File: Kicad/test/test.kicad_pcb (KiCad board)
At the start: 2 copper layers, 50 x 50 mm, 69 parts, among them J1 SPKOUT, J2 PrgmUART, P1 USB_C_Plug_USB2.0, SW1 SW_Push, SW2 SW_Push, SW3 SW_Push, SW4 SW_Push, SW5 SW_Push, U1 MAX98357A, U2 ESP32-S3-WROOM-1

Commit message: Started PCB Layout designs
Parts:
- moved SW2 0.45 mm to (159.5, 120.5)
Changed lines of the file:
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@@
 	(footprint "switchLibrary:K2-1114SA-A4SW-06"
 		(layer "F.Cu")
-		(at 159.898871 120.51318 -150)
+		(at 159.455129 120.467423 -150)
 		(property "Reference" "SW2"
 			(at 0 -3.83 30)

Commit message: Placed components on PCB
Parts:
- C1, C10, C11, C12, C13, C14, C15, C16, C17, C18, C19, C2, C20, C21, C22, C23, C24, C25, C26, C27, C28, C29, C3, C30, C4, C5, C6, C7, C8, C9, L1, L2: footprint Capacitor_SMD:C_0805_2012Metric_Pad1.18x1.45mm_HandSolder -> Capacitor_SMD:C_0603_1608Metric_Pad1.08x0.95mm_HandSolder
- J2: footprint Connector_PinHeader_2.54mm:PinHeader_1x06_P2.54mm_Vertical -> Connector_PinHeader_2.54mm:PinHeader_2x03_P2.54mm_Vertical
- R1, R10, R11, R12, R13, R14, R15, R16, R2, R3, R4, R5, R6, R7, R8, R9: footprint Resistor_SMD:R_0805_2012Metric_Pad1.20x1.40mm_HandSolder -> Resistor_SMD:R_0603_1608Metric_Pad0.98x0.95mm_HandSolder
- moved C11 125.2 mm to (164.0, 105.7), turned to -90 degrees
- moved C29 122.5 mm to (157.0, 117.0)
- moved C10 122.2 mm to (162.7, 99.6), turned to 90 degrees
- moved C12 120.4 mm to (163.1, 102.5), turned to 180 degrees
- moved C6 118.9 mm to (155.2, 112.7), turned to 180 degrees
- moved C7 118.1 mm to (157.9, 111.5), turned to -90 degrees
- moved C28 117.1 mm to (143.8, 116.5), turned to 180 degrees
- moved C1 113.6 mm to (154.2, 90.9), turned to 180 degrees
- moved C8 113.4 mm to (155.2, 110.4), turned to 180 degrees
- moved NC2 112.1 mm to (150.1, 106.3)
- moved C26 112.0 mm to (159.3, 114.5)
- moved C9 111.2 mm to (164.3, 96.7), turned to 180 degrees
- moved C23 108.7 mm to (160.2, 99.6), turned to -90 degrees
- moved C27 108.0 mm to (151.7, 119.6)
- moved C3 107.6 mm to (155.6, 85.4), turned to 90 degrees
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
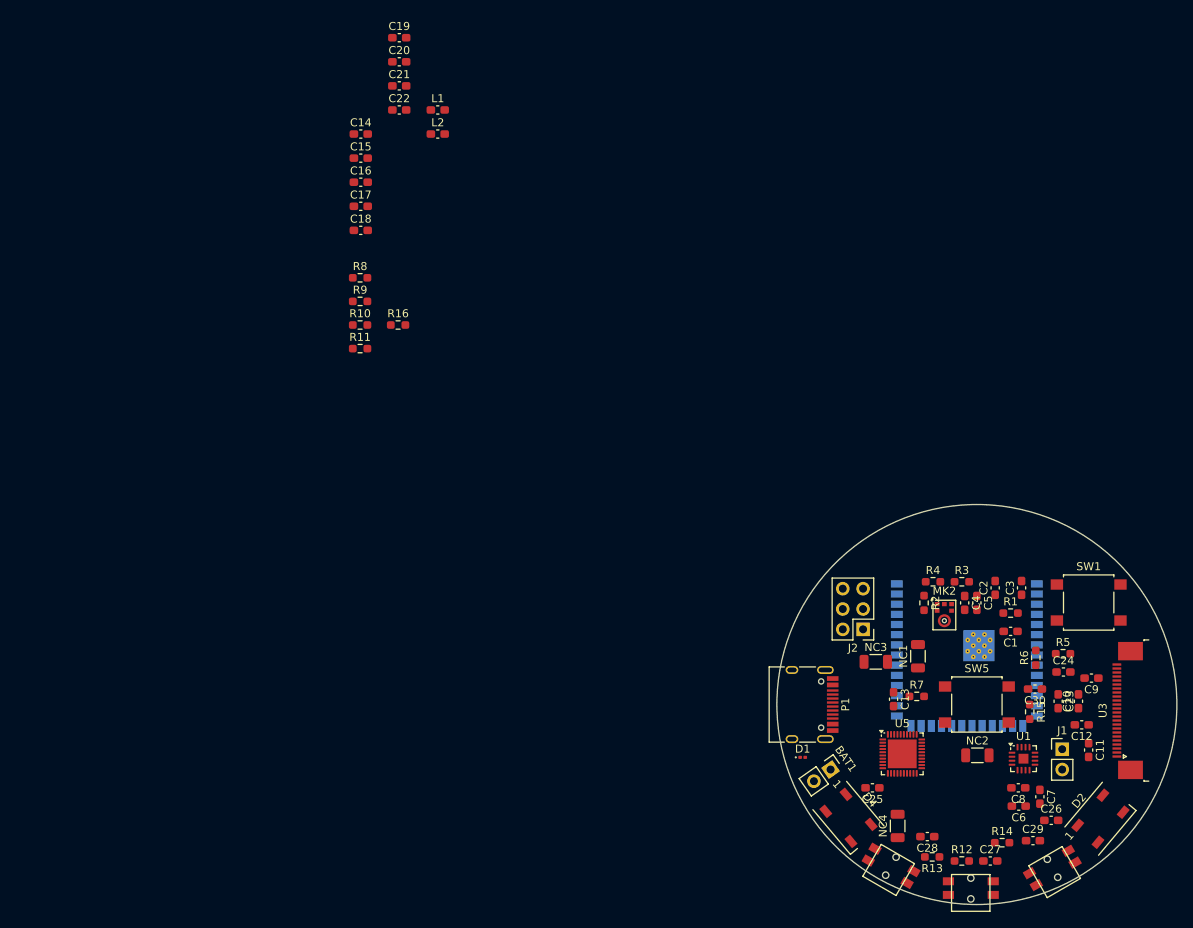
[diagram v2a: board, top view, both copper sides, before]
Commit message: 3d Model Casing and PCB Added
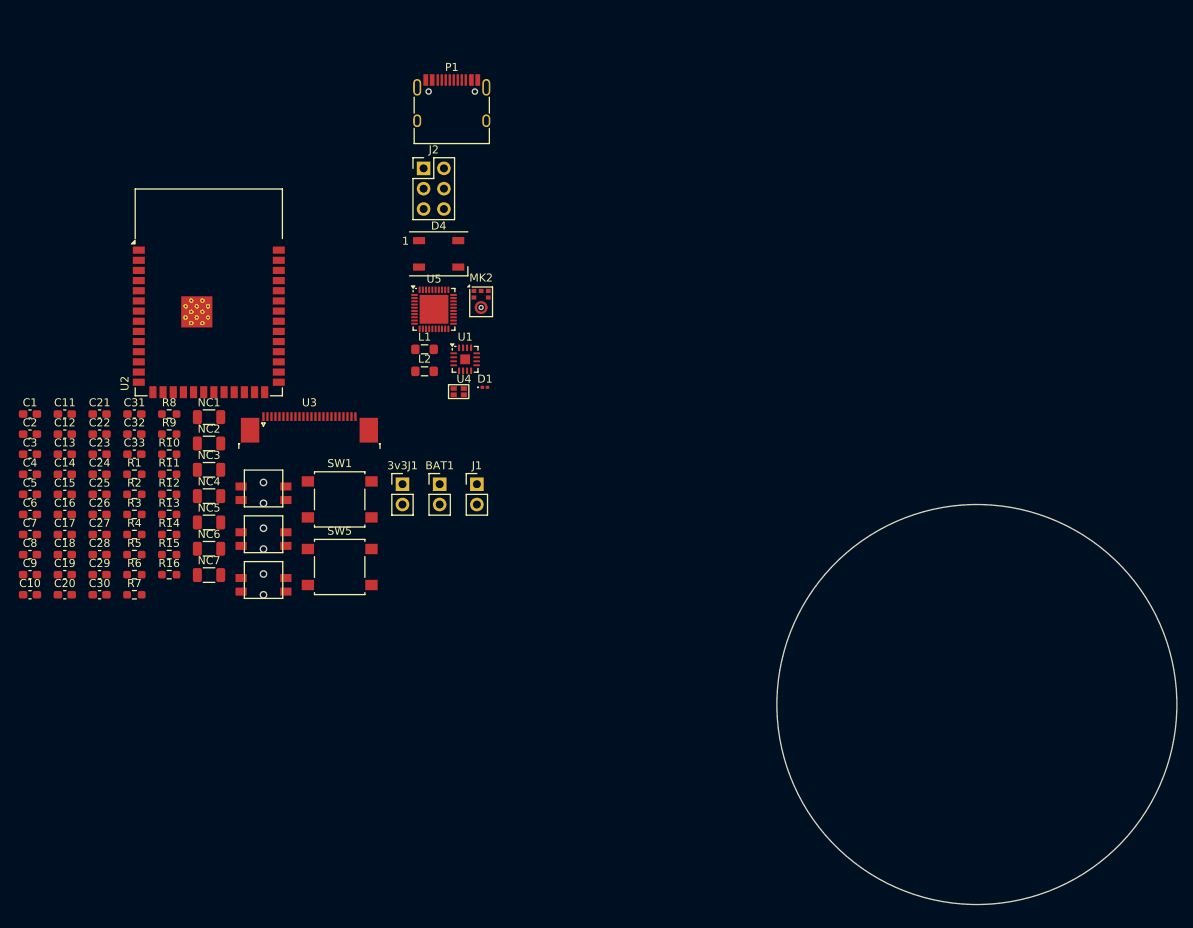
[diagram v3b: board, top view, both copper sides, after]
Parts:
- removed D2: WS2812B, LED_SMD:LED_WS2812B_PLCC4_5.0x5.0mm_P3.2mm
- added 3v3J1: Conn_01x02_Pin, Connector_PinHeader_2.54mm:PinHeader_1x02_P2.54mm_Vertical, F.Cu at (78.2, 72.5)
- added C31: 100n, Capacitor_SMD:C_0603_1608Metric_Pad1.08x0.95mm_HandSolder, F.Cu at (44.7, 63.7)
- added C32: 100n, Capacitor_SMD:C_0603_1608Metric_Pad1.08x0.95mm_HandSolder, F.Cu at (44.7, 66.2)
- added C33: 15p, Capacitor_SMD:C_0603_1608Metric_Pad1.08x0.95mm_HandSolder, F.Cu at (44.7, 68.7)
- added NC5: 0, Resistor_SMD:R_1206_3216Metric, F.Cu at (54.0, 77.2)
- added NC6: 0, Resistor_SMD:R_1206_3216Metric, F.Cu at (54.0, 80.5)
- added NC7: 0, Resistor_SMD:R_1206_3216Metric, F.Cu at (54.0, 83.8)
- added U4: 24Mhz, Footprint_Wareit_Mic:YSO110TR, F.Cu at (85.3, 60.8)
- L1, L2: footprint Capacitor_SMD:C_0603_1608Metric_Pad1.08x0.95mm_HandSolder -> Inductor_SMD:L_0805_2012Metric_Pad1.05x1.20mm_HandSolder
- U2: moved to F.Cu
- U3: value ~ -> OV5640
- U5: value ~ -> AXP2101
- moved C11 134.7 mm to (36.0, 63.7), turned to 0 degrees
- moved C9 133.3 mm to (31.6, 83.8), turned to 0 degrees
- moved C12 132.2 mm to (36.0, 66.2), turned to 0 degrees
- moved C10 131.7 mm to (31.6, 86.3), turned to 0 degrees
- moved C7 130.4 mm to (31.6, 78.8), turned to 0 degrees
- moved C6 128.9 mm to (31.6, 76.2), turned to 0 degrees
- moved C8 126.9 mm to (31.6, 81.3), turned to 0 degrees
- moved C1 125.6 mm to (31.6, 63.7), turned to 0 degrees
- moved C3 125.1 mm to (31.6, 68.7), turned to 0 degrees
- moved C26 125.0 mm to (40.3, 76.2)
- moved C23 123.7 mm to (40.3, 68.7), turned to 0 degrees
- moved C24 123.0 mm to (40.3, 71.2)
- moved C2 122.2 mm to (31.6, 66.2), turned to 0 degrees
- moved C29 121.3 mm to (40.3, 83.8)
- moved C5 119.1 mm to (31.6, 73.7), turned to 0 degrees
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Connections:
- net VCAM3V3 renamed +3V3CAM
- C19 pad 2: +3V3 -> Net-(U5-FB1)
- D4 pad 2: Net-(D2-DIN) -> unconnected-(D4-DOUT-Pad2)
- L1 pad 2: +3V3 -> Net-(U5-FB1)
- U3 pad 13: CAM_MCLK -> Net-(U3-MCLK)
- U5 pad 21: +3V3 -> Net-(U5-FB1)

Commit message: Floorplanning done
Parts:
- removed SW1: SW_Push, Button_Switch_SMD:SW_SPST_B3S-1000
- 3v3J1, BAT1, C14, C15, C16, C17, C18, C19, C20, C21, C22, D1, L1, L2, NC5, P1, R10, R11, R16, R8, R9, U2, U5: moved to B.Cu
- moved C28 130.8 mm to (170.7, 91.9), turned to 90 degrees
- moved C14 130.4 mm to (165.1, 89.6), turned to 180 degrees
- moved C16 127.3 mm to (161.3, 98.2), turned to 180 degrees
- moved C21 125.2 mm to (161.2, 96.4), turned to 180 degrees
- moved C18 124.5 mm to (159.8, 94.8), turned to 180 degrees
- moved C11 124.3 mm to (157.4, 90.6)
- moved C17 123.5 mm to (157.7, 99.4)
- moved C12 123.5 mm to (157.4, 88.8)
- moved C19 121.9 mm to (157.2, 96.5), turned to 90 degrees
- moved C15 121.5 mm to (157.0, 84.3), turned to -90 degrees
- moved R13 119.7 mm to (167.5, 93.0)
- moved C24 119.4 mm to (158.8, 86.3), turned to 90 degrees
- moved C25 119.1 mm to (157.7, 94.0)
- moved C26 119.0 mm to (157.7, 95.8)
- moved C2 117.9 mm to (140.9, 110.3)
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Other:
- board size 50 x 50 mm -> 48 x 48 mm
- board text added: "Battery"

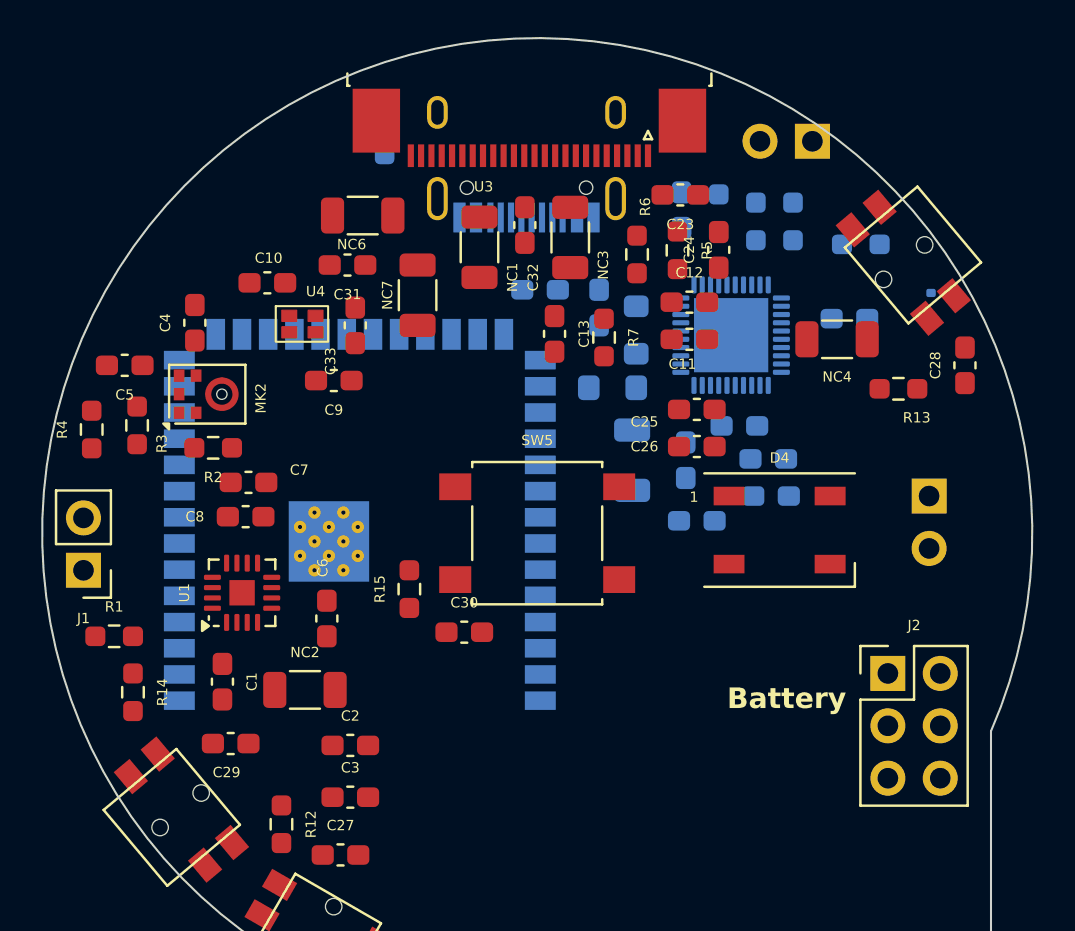
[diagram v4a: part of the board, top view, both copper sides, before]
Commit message: Started PCB routing
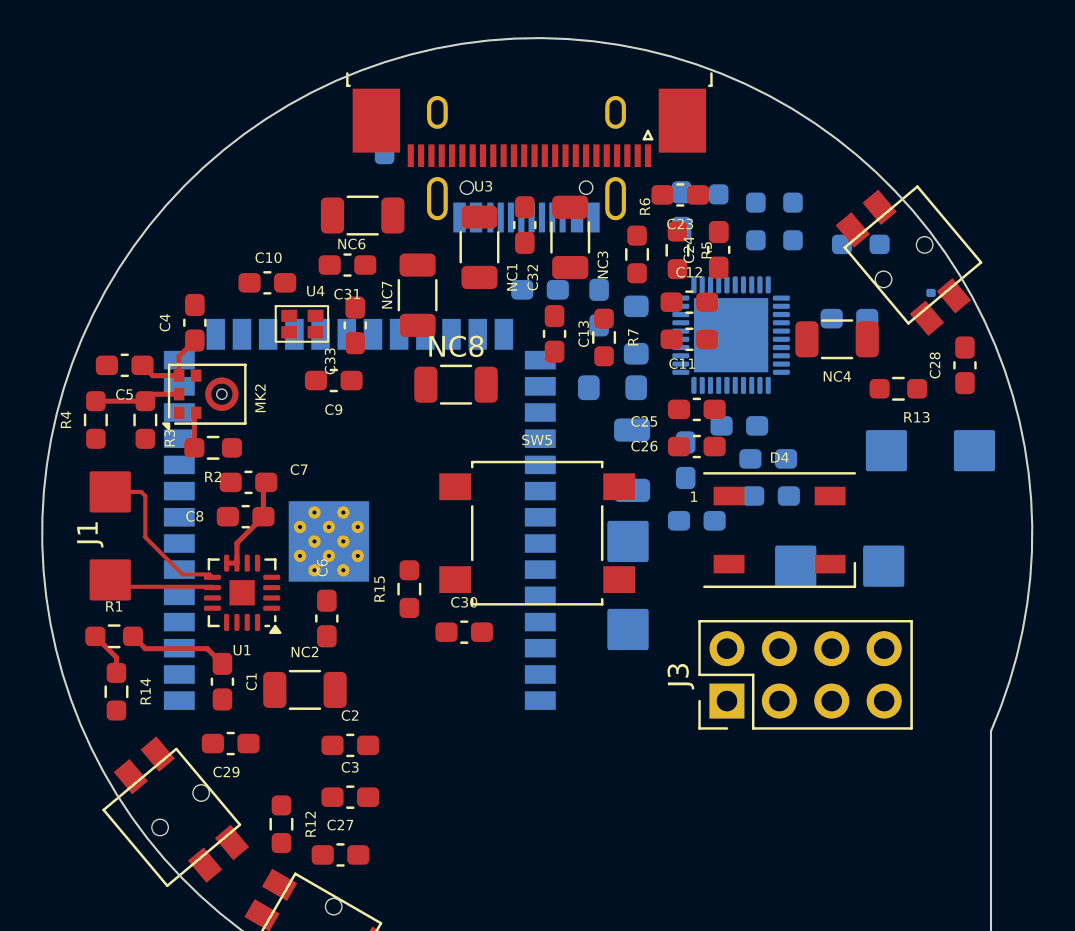
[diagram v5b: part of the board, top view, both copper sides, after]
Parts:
- removed J2: PrgmUART, Connector_PinHeader_2.54mm:PinHeader_2x03_P2.54mm_Vertical
- added 3v3J2: Conn_01x02_Pin, Footprint_Wareit_Mic:SMD_CONNECTOR_PAD, B.Cu at (164.7, 101.7)
- added J3: Conn_01x08_Pin, Connector_PinHeader_2.54mm:PinHeader_2x04_P2.54mm_Vertical, F.Cu at (159.2, 108.1)
- added NC8: 0, Resistor_SMD:R_1206_3216Metric, F.Cu at (146.1, 92.8)
- 3v3J1, BAT1, J1: footprint Connector_PinHeader_2.54mm:PinHeader_1x02_P2.54mm_Vertical -> Footprint_Wareit_Mic:SMD_CONNECTOR_PAD
- moved BAT1 23.3 mm to (154.3, 102.5)
- moved 3v3J1 2.15 mm to (169.1, 96.1)
- moved J1 2.14 mm to (129.3, 100.1), turned to 90 degrees
- moved R14 0.80 mm to (129.6, 107.7)
- moved R4 0.50 mm to (128.6, 94.5)
- moved R3 0.48 mm to (131.0, 94.5)
- turned U1 to 180 degrees
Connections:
- U2 pad 25: unconnected-(U2-IO48-Pad25) -> Net-(U2-IO48)
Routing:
- net SPK_P: track 0.00 -> 7.84 mm
- net +3V3: track 0.00 -> 6.20 mm
- net SPK_N: track 0.00 -> 5.11 mm
- net VSYS: track 0.00 -> 5.00 mm
- net EN: track 0.00 -> 4.89 mm
- net Net-(MK2-SD): track 0.00 -> 4.18 mm
- net Net-(MK2-LR): track 0.00 -> 1.73 mm

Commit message: Updated schematics
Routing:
- net SW_L1: track 0.00 -> 13.1 mm
- net Net-(U1-GAIN_SLOT): track 0.00 -> 6.16 mm
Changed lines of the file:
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@@
 		)
 		(fp_text user "${REFERENCE}"
-			(at 1.27 3.81 360)
+			(at 1.27 3.81 0)
 			(layer "F.Fab")
 			(effects
@@
 		(tags "TQFN NoLead")
 		(property "Reference" "U1"
-			(at 0 -2.8 360)
+			(at 0 -2.8 0)
 			(layer "F.SilkS")
 			(effects
@@
 		)
 		(property "Value" "MAX98357A"
-			(at 0 2.8 360)
+			(at 0 2.8 0)
 			(layer "F.Fab")
 			(effects
@@
 		)
 		(fp_text user "${REFERENCE}"
-			(at 0 0 360)
+			(at 0 0 0)
 			(layer "F.Fab")
 			(effects
@@
 		(tags "resistor")
 		(property "Reference" "NC8"
-			(at 0 -1.82 360)
+			(at 0 -1.82 0)
 			(layer "F.SilkS")
 			(effects
@@
 		)
 		(property "Value" "0"
-			(at 0 1.82 360)
+			(at 0 1.82 0)
 			(layer "F.Fab")
 			(effects
@@
 		)
 		(fp_text user "${REFERENCE}"
-			(at 0 0 360)
+			(at 0 0 0)
 			(layer "F.Fab")
 			(effects
@@
 	)
 	(segment
+		(start 146.025 102.25)
+		(end 153.975 102.25)
+		(width 0.25)
+		(layer "F.Cu")
+		(net 14)
+	)
+	(segment
+		(start 146.025 104.375)
+		(end 145.6 104.8)
+		(width 0.25)
+		(layer "F.Cu")
+		(net 14)
+	)
+	(segment
+		(start 144.25 102.25)
+		(end 146.025 102.25)
+		(width 0.25)
+		(layer "F.Cu")
+		(net 14)
+	)
+	(segment
+		(start 146.025 102.25)
+		(end 146.025 104.375)
+		(width 0.25)
+		(layer "F.Cu")
+		(net 14)
+	)
+	(segment
+		(start 143.8 101.8)
+		(end 144.25 102.25)
+		(width 0.25)
+		(layer "F.Cu")
+		(net 14)
+	)
+	(segment
 		(start 132.8 102)
 		(end 134.1125 102)
@@
 	)
 	(segment
+		(start 138.34 103.14)
+		(end 138.4 103.2)
+		(width 0.25)
+		(layer "F.Cu")
+		(net 29)
+	)
+	(segment
+		(start 137.1275 103.14)
+		(end 138.34 103.14)
+		(width 0.25)
+		(layer "F.Cu")
+		(net 29)
+	)
+	(segment
+		(start 138.4 105.2)
+		(end 138.4 103.2)
+		(width 0.25)
+		(layer "F.Cu")
+		(net 29)
+	)
+	(segment
+		(start 137.275 106.325)
+		(end 138.4 105.2)
+		(width 0.25)
+		(layer "F.Cu")
+		(net 29)
+	)
+	(segment
+		(start 137.275 107.6)
+		(end 137.275 106.325)
+		(width 0.25)
+		(layer "F.Cu")
+		(net 29)
+	)
+	(segment

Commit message: Updated PCB floor
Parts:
- R5, R6, R8, R9: value 4.7k -> 10k
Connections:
- R8 pad 1: PMIC_SCL -> CAM_SCL
- R9 pad 1: PMIC_SDA -> CAM_SDA
- U2 pad 10: CAM_SCL -> SW_L1
- U2 pad 11: CAM_SDA -> SW_L2
- U2 pad 22: PMIC_SCL -> CAM_SCL
- U2 pad 28: PMIC_PWROK -> unconnected-(U2-IO35-Pad28)
- U2 pad 29: SW_L1 -> unconnected-(U2-IO36-Pad29)
- U2 pad 30: SW_L2 -> unconnected-(U2-IO37-Pad30)
- U2 pad 8: PMIC_SDA -> CAM_SDA
- U5 pad 29: PMIC_PWROK -> unconnected-(U5-PWROK-Pad29)
- U5 pad 39: PMIC_SDA -> CAM_SDA
- U5 pad 40: PMIC_SCL -> CAM_SCL
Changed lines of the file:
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@@
 	(net 40 "CAM_SDA")
 	(net 41 "CAM_SCL")
-	(net 42 "PMIC_SCL")
-	(net 43 "PMIC_SDA")
+	(net 42 "unconnected-(U2-IO35-Pad28)")
+	(net 43 "unconnected-(U2-IO36-Pad29)")
 	(net 44 "PMIC_IRQ")
 	(net 45 "unconnected-(U1-NC-Pad6)")
@@
 	(net 64 "Net-(U2-IO48)")
 	(net 65 "CAM_Y2")
-	(net 66 "PMIC_PWROK")
+	(net 66 "unconnected-(U2-IO37-Pad30)")
 	(net 67 "CAM_HREF")
 	(net 68 "CAM_Y7")
@@
 	(net 94 "Net-(U3-MCLK)")
 	(net 95 "unconnected-(U4-OE-Pad1)")
+	(net 96 "unconnected-(U5-PWROK-Pad29)")
 	(footprint "Capacitor_SMD:C_0603_1608Metric_Pad1.08x0.95mm_HandSolder"
 		(layer "F.Cu")
@@
 			)
 		)
-		(property "Value" "4.7k"
+		(property "Value" "10k"
 			(at -0.1375 9.6925 90)
 			(layer "F.Fab")
@@
 			)
 		)
-		(property "Value" "4.7k"
+		(property "Value" "10k"
 			(at 0 1.43 90)
 			(layer "F.Fab")
@@
 			(size 1.5 0.9)
 			(layers "B.Cu" "B.Paste" "B.Mask")
-			(net 43 "PMIC_SDA")
+			(net 40 "CAM_SDA")
 			(pinfunction "IO15")
 			(pintype "bidirectional")
@@
 			(size 1.5 0.9)
 			(layers "B.Cu" "B.Paste" "B.Mask")
-			(net 41 "CAM_SCL")
+			(net 14 "SW_L1")
 			(pinfunction "IO17")
 			(pintype "bidirectional")
@@
 			(size 1.5 0.9)
 			(layers "B.Cu" "B.Paste" "B.Mask")
-			(net 40 "CAM_SDA")
+			(net 13 "SW_L2")
 			(pinfunction "IO18")
 			(pintype "bidirectional")
@@
 			(size 1.5 0.9)
 			(layers "B.Cu" "B.Paste" "B.Mask")
-			(net 42 "PMIC_SCL")
+			(net 41 "CAM_SCL")
 			(pinfunction "IO14")
 			(pintype "bidirectional")
@@
 			(size 1.5 0.9)
 			(layers "B.Cu" "B.Paste" "B.Mask")
-			(net 66 "PMIC_PWROK")
+			(net 42 "unconnected-(U2-IO35-Pad28)")
 			(pinfunction "IO35")
-			(pintype "bidirectional")
+			(pintype "bidirectional+no_connect")
 		)
 		(pad "29" smd rect
@@
 			(size 1.5 0.9)
 			(layers "B.Cu" "B.Paste" "B.Mask")
-			(net 14 "SW_L1")
+			(net 43 "unconnected-(U2-IO36-Pad29)")
 			(pinfunction "IO36")
-			(pintype "bidirectional")
+			(pintype "bidirectional+no_connect")
 		)
 		(pad "30" smd rect
@@
 			(size 1.5 0.9)
 			(layers "B.Cu" "B.Paste" "B.Mask")
-			(net 13 "SW_L2")
+			(net 66 "unconnected-(U2-IO37-Pad30)")
 			(pinfunction "IO37")
-			(pintype "bidirectional")
+			(pintype "bidirectional+no_connect")
 		)
 		(pad "31" smd rect
@@
 			)
 		)
-		(property "Value" "4.7k"
+		(property "Value" "10k"
 			(at 0 -1.43 90)
 			(layer "B.Fab")
@@
 			(layers "B.Cu" "B.Paste" "B.Mask")
 			(roundrect_rratio 0.25)
-			(net 43 "PMIC_SDA")
+			(net 40 "CAM_SDA")
 			(pintype "passive")
 		)
@@
 			(layers "B.Cu" "B.Paste" "B.Mask")
 			(roundrect_rratio 0.25)
-			(net 66 "PMIC_PWROK")
+			(net 96 "unconnected-(U5-PWROK-Pad29)")
 			(pinfunction "PWROK")
-			(pintype "output")
+			(pintype "output+no_connect")
 		)
 		(pad "30" smd roundrect
@@
 			(layers "B.Cu" "B.Paste" "B.Mask")
 			(roundrect_rratio 0.25)
-			(net 43 "PMIC_SDA")
+			(net 40 "CAM_SDA")
 			(pinfunction "SDA")
 			(pintype "bidirectional")
@@
 			(layers "B.Cu" "B.Paste" "B.Mask")
 			(roundrect_rratio 0.25)
-			(net 42 "PMIC_SCL")
+			(net 41 "CAM_SCL")
 			(pinfunction "SCK")
 			(pintype "input")
@@
 			)
 		)
-		(property "Value" "4.7k"
+		(property "Value" "10k"
 			(at 0 -1.43 90)
 			(layer "B.Fab")
@@
 			(layers "B.Cu" "B.Paste" "B.Mask")
 			(roundrect_rratio 0.25)
-			(net 42 "PMIC_SCL")
+			(net 41 "CAM_SCL")
 			(pintype "passive")
 		)
